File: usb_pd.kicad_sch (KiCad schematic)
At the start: 37 parts, among them J1 USB-C_GCT_USB4105-GF-A, J2 JST_SH_1x4_SM04B-SRSS-TB-LF-SN, Q1 SQS401EN-T1_BE3, U1 STUSB4500_QFN, U5 TPD4E02B04DQA, U6 TPD4E02B04DQA

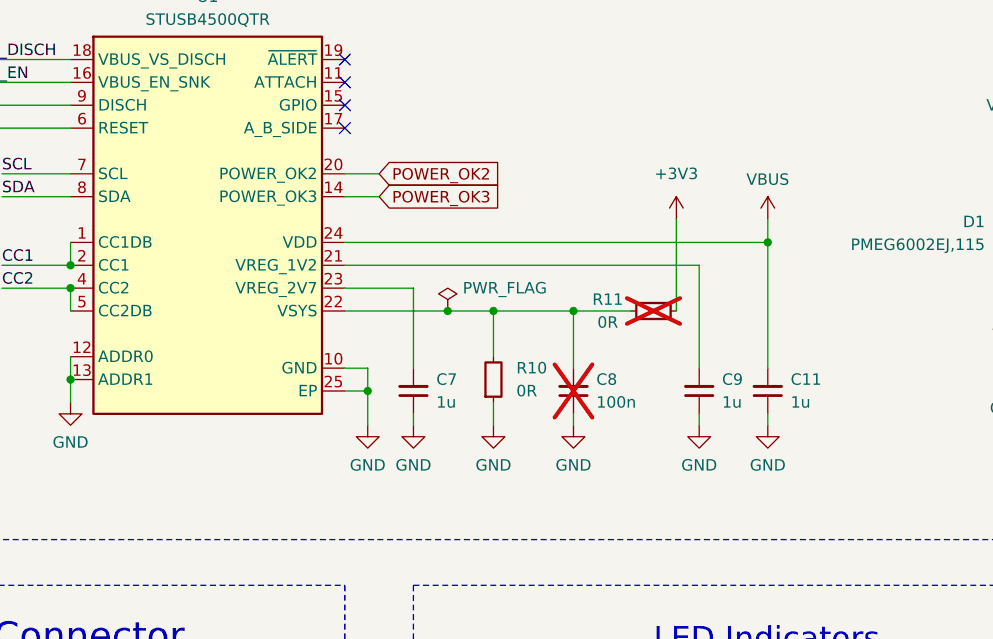
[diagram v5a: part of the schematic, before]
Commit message: [#57006] Remove R11, C8
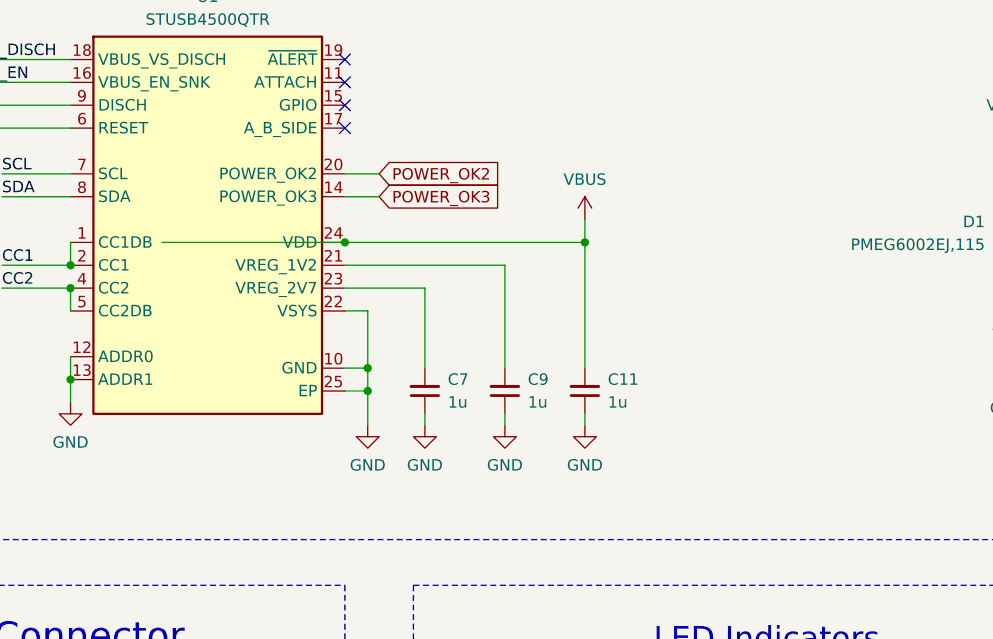
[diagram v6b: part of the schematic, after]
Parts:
- removed C8: C_100n_0402, antmicro-footprints:C_0402_1005Metric, symbol antmicroCapacitors0402:C_100n_0402
- removed R10, R11: R_0R_0402, antmicro-footprints:R_0402_1005Metric, symbol antmicroResistors0402:R_0R_0402
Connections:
- net GND: now also U1.22 (VSYS)
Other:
- moved on the sheet: C11, C7, C9
